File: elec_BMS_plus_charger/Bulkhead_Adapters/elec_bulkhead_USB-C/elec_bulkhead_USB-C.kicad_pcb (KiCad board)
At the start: 2 copper layers, 94 x 41 mm, 51 parts, among them J1 JST EH 2, J13 Dynamixel-3, J14 Dynamixel-3, J2 JST SH, J7 JST SH, Q1 BSZ034N04LS, Q2 BSZ034N04LS, U1 HY2120, U2 BQ25887RGE

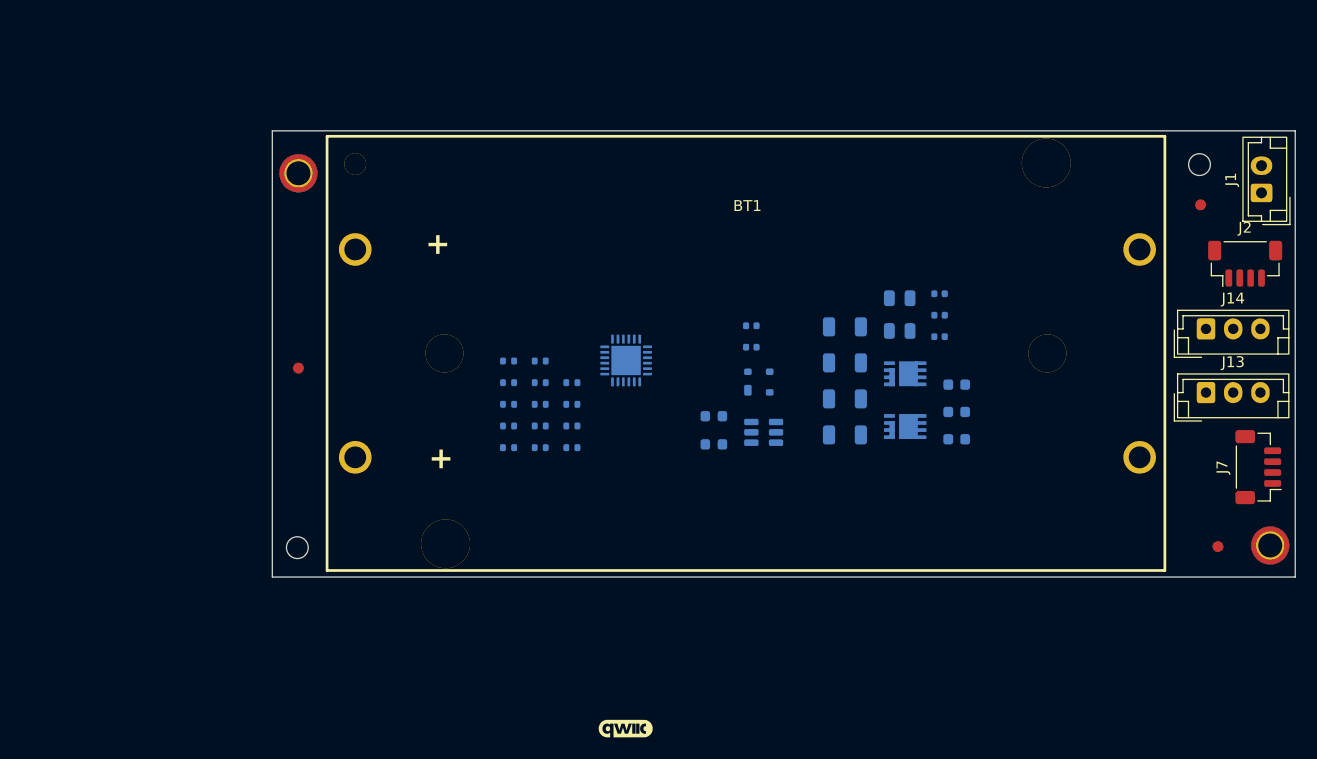
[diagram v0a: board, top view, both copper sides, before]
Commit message: [update] BMS schematic DRC 0k.
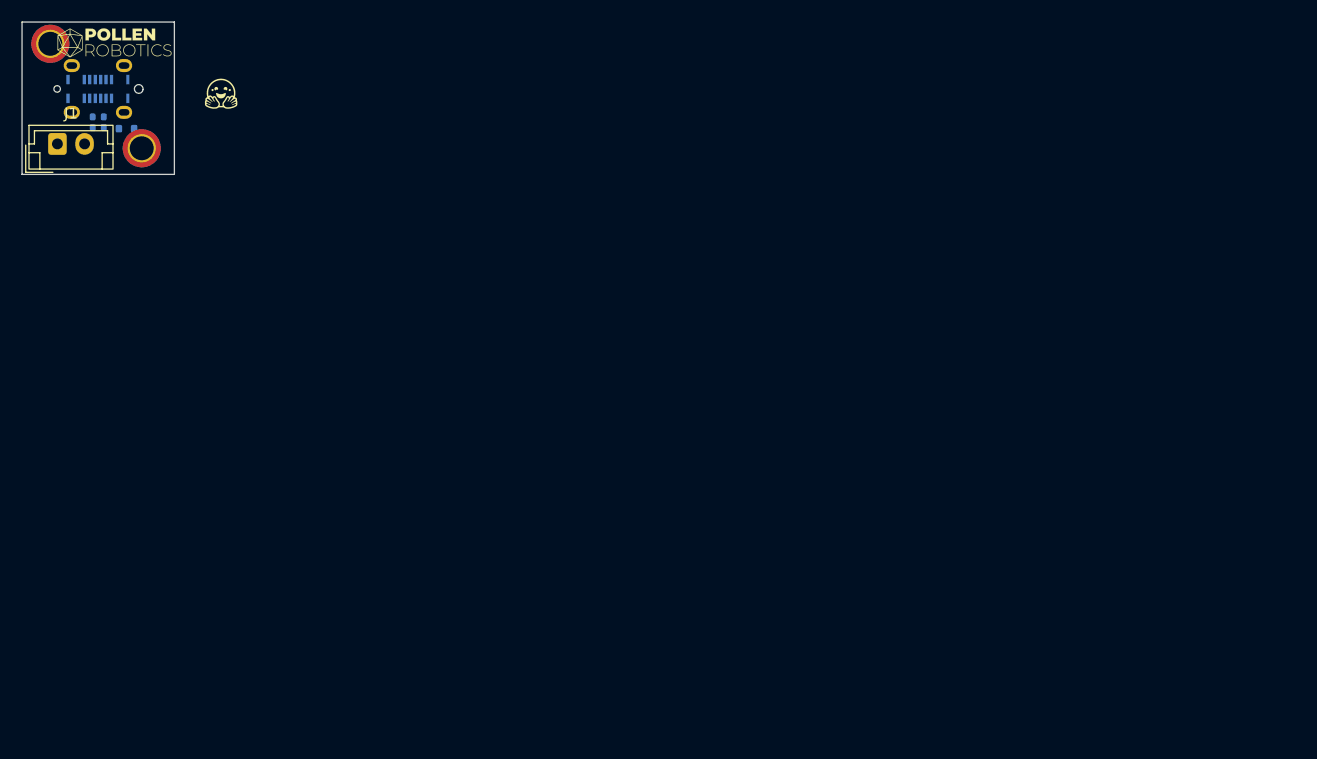
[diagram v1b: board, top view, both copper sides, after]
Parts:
- removed BT1: BH-18650-A1BJ021, LCSC_parts_lib:BAT-TH_L77.0-W39.9_BH-18650-A1BJ021
- removed C1, C2: 100n, Capacitor_SMD:C_0402_1005Metric
- removed C3, L1: 1u, Capacitor_SMD:C_0402_1005Metric
- removed C4, C6: 10u, Capacitor_SMD:C_0603_1608Metric
- removed C5: 47n, Capacitor_SMD:C_0402_1005Metric
- removed C7: 4u7, Capacitor_SMD:C_0603_1608Metric
- removed C8, C9: 22u low ESR, Capacitor_SMD:C_0805_2012Metric
- removed D1: SP0503BAHT, Package_TO_SOT_SMD:SOT-143
- removed D2: Orange, LED_SMD:LED_0603_1608Metric
- removed FID1, FID2, FID3: DNP Fiducial, Fiducial:Fiducial_1mm_Mask2mm
- removed G1: qwiic_Logo, Library_Pollen:Logo_qwiic_5mm
- removed H6, H7: Centering Hole 2 mm, Library_Pollen:MountingHole_2.0mm
- removed J13, J14: Dynamixel-3, Connector_JST:JST_EH_B3B-EH-A_1x03_P2.50mm_Vertical
- removed J7: JST SH, Connector_JST:JST_SH_BM04B-SRSS-TB_1x04-1MP_P1.00mm_Vertical
- removed Q1, Q2: BSZ034N04LS, Library_Pollen:PQFN_3.3x3.3mm_-_PG-TDSON-8_FL
- removed R10, R7, R8, R9: 62R-0,25W, Resistor_SMD:R_1206_3216Metric
- removed R11: 5,23k, Resistor_SMD:R_0402_1005Metric
- removed R12: 30k1, Resistor_SMD:R_0402_1005Metric
- removed R13, R14: 3k3, Resistor_SMD:R_0402_1005Metric
- removed R15, TH1: 10k, Resistor_SMD:R_0402_1005Metric
- removed R16, R17: 0R, Resistor_SMD:R_0402_1005Metric
- removed R3: 2k, Resistor_SMD:R_0402_1005Metric
- removed R4: 330R, Resistor_SMD:R_0402_1005Metric
- removed R5, R6: DNP-10k, Resistor_SMD:R_0402_1005Metric
- removed U1: HY2120, Package_TO_SOT_SMD:SOT-23-6
- removed U2: BQ25887RGE, Package_DFN_QFN:Texas_RGE0024H_VQFN-24-1EP_4x4mm_P0.5mm_EP2.7x2.7mm
- D3: value Green -> ESD5Z6.0; footprint LED_SMD:LED_0603_1608Metric -> Diode_SMD:D_SOD-523
- H2, H3: moved to F.Cu
- J2: value JST SH -> USB-C Rec. Vert.; footprint Connector_JST:JST_SH_BM04B-SRSS-TB_1x04-1MP_P1.00mm_Vertical -> Library_Pollen:USB-C_16p_vert_Shou-Han_TYPE-C 16P LTH6.8 - C5187468; moved to B.Cu
- R1, R2: value 330R -> 5k1
- moved J1 110.7 mm to (82.1, 55.8), turned to 0 degrees
- moved H5 109.9 mm to (89.9, 56.2)
- moved J2 106.6 mm to (85.9, 50.8)
- moved D3 60.1 mm to (88.5, 54.4)
- moved R1 48.4 mm to (85.9, 53.4), turned to 180 degrees
- moved R2 46.6 mm to (85.9, 54.3), turned to 180 degrees
- moved H2 39.8 mm to (97.2, 51.2), turned to 0 degrees
- moved H3 36.2 mm to (87.3, 44.8), turned to 0 degrees
- moved H4 25.7 mm to (81.5, 46.6)
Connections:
- D3 pad 2: +BATT -> GND
- J1 pad 2: +5V -> Net-(D3-K)
- R1 pad 1: +BATT -> Net-(J2-CC1)
- R1 pad 2: Net-(U1-Vdd) -> GND
- R2 pad 1: /Power/MID -> Net-(J2-CC2)
- R2 pad 2: Net-(U1-VC) -> GND
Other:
- board size 94 x 41 mm -> 14 x 14 mm
